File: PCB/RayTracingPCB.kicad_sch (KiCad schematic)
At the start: 8 parts, among them J1 Conn_ARM_JTAG_SWD_10

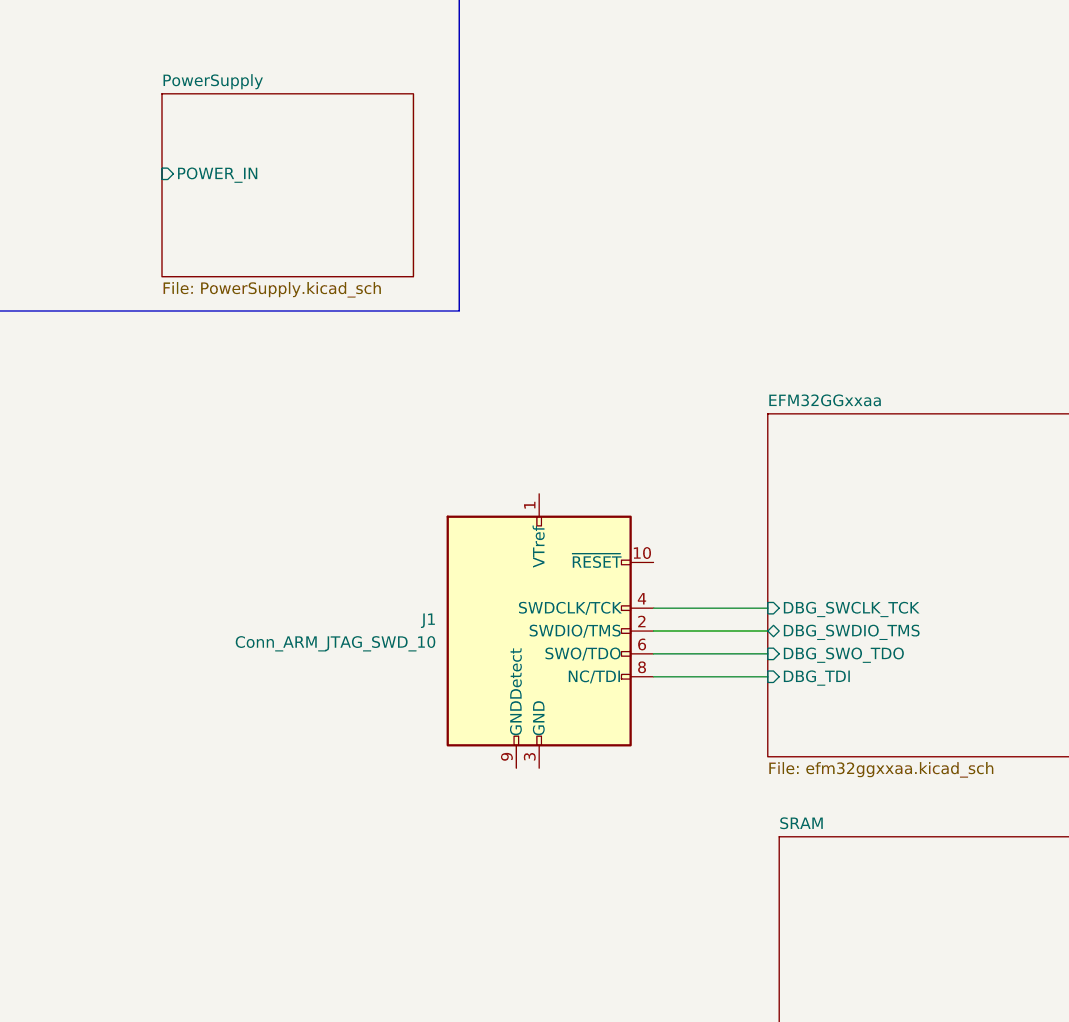
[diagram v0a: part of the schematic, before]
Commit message: add barrel jack
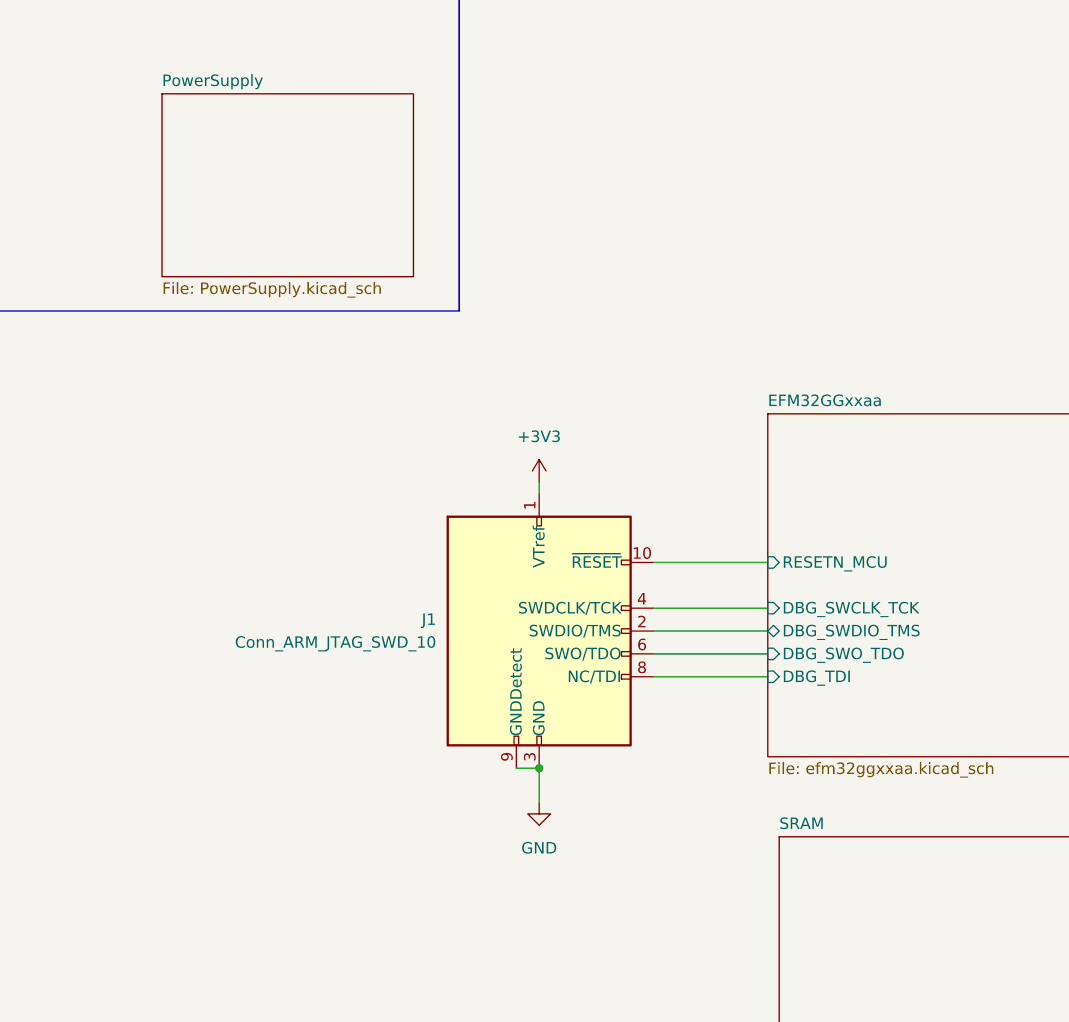
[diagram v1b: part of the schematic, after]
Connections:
- net +3V3: now reaches J1.1 (VTref)
- net EFM32GGxxaa/RESETN_MCU: now reaches J1.10 (~{RESET})
- net GND: now reaches J1.3 (GND), J1.5 (GND)
- net GND: now also J1.9 (GNDDetect)
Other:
- sheet EFM32GGxxaa ports: added RESETN_MCU; removed none
- sheet PowerSupply ports: added none; removed POWER_IN
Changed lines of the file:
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@@
   (junction (at 220.98 90.17) (diameter 0) (color 162 255 50 1)
   )
+  (junction (at 88.9 109.22) (diameter 0) (color 0 0 0 0)
+  )
   (junction (at 218.44 93.98) (diameter 0) (color 0 0 0 0)
   )
@@
   )
   (junction (at 210.82 101.6) (diameter 0) (color 0 0 0 0)
+  )
+  (wire (pts (xy 86.36 109.22) (xy 88.9 109.22))
+    (stroke (width 0) (type default))
   )
   (wire (pts (xy 220.98 90.17) (xy 236.22 90.17))
@@
     (stroke (width 0) (type default))
   )
+  (wire (pts (xy 88.9 77.47) (xy 88.9 78.74))
+    (stroke (width 0) (type default))
+  )
   (wire (pts (xy 213.36 99.06) (xy 236.22 99.06))
     (stroke (width 0) (type default))
@@
     (stroke (width 0) (type default) (color 91 55 255 1))
   )
+  (wire (pts (xy 101.6 86.36) (xy 114.3 86.36))
+    (stroke (width 0) (type default))
+  )
   (wire (pts (xy 220.98 90.17) (xy 220.98 130.81))
     (stroke (width 0) (type default) (color 162 255 50 1))
@@
   (wire (pts (xy 173.99 83.82) (xy 236.22 83.82))
     (stroke (width 0) (type default) (color 91 55 255 1))
+  )
+  (wire (pts (xy 88.9 109.22) (xy 88.9 113.03))
+    (stroke (width 0) (type default))
   )
   (wire (pts (xy 45.72 181.61) (xy 68.58 181.61))
@@
   (label "EMF32GG_QSPI0_IO0" (at 45.72 177.8 0) (fields_autoplaced)
     (effects (font (size 1.27 1.27)) (justify left bottom))
+  )
+  (symbol (lib_id "power:+3V3") (at 88.9 77.47 0) (unit 1)
+    (in_bom yes) (on_board yes) (dnp no) (fields_autoplaced)
+    (property "Reference" "#PWR066" (at 88.9 81.28 0)
+      (effects (font (size 1.27 1.27)) hide)
+    )
+    (property "Value" "+3V3" (at 88.9 72.39 0)
+      (effects (font (size 1.27 1.27)))
+    )
+    (property "Footprint" "" (at 88.9 77.47 0)
+      (effects (font (size 1.27 1.27)) hide)
+    )
+    (property "Datasheet" "" (at 88.9 77.47 0)
+      (effects (font (size 1.27 1.27)) hide)
+    )
+    (pin "1")
+    (instances
+      (project "RayTracingPCB"
+        (path "/e9047d94-28be-4266-894b-6ee25ef088bd"
+          (reference "#PWR066") (unit 1)
+        )
+      )
+    )
+  )
+  (symbol (lib_id "power:GND") (at 88.9 113.03 0) (unit 1)
+    (in_bom yes) (on_board yes) (dnp no) (fields_autoplaced)
+    (property "Reference" "#PWR067" (at 88.9 119.38 0)
+      (effects (font (size 1.27 1.27)) hide)
+    )
+    (property "Value" "GND" (at 88.9 118.11 0)
+      (effects (font (size 1.27 1.27)))
+    )
+    (property "Footprint" "" (at 88.9 113.03 0)
+      (effects (font (size 1.27 1.27)) hide)
+    )
+    (property "Datasheet" "" (at 88.9 113.03 0)
+      (effects (font (size 1.27 1.27)) hide)
+    )
+    (pin "1")
+    (instances
+      (project "RayTracingPCB"
+        (path "/e9047d94-28be-4266-894b-6ee25ef088bd"
+          (reference "#PWR067") (unit 1)
+        )
+      )
+    )
   )
   (symbol (lib_id "Connector:TestPoint_Probe") (at 68.58 185.42 0) (unit 1)
@@
       (effects (font (size 1.27 1.27)) (justify right top) hide)
     )
-    (pin "POWER_IN" input (at 46.99 43.18 180)
-      (effects (font (size 1.27 1.27)) (justify left))
-    )
     (instances
       (project "RayTracingPCB"
@@
       (effects (font (size 1.27 1.27)) (justify right))
     )
-    (instances
+    (pin "RESETN_MCU" input (at 114.3 86.36 180)
+      (effects (font (size 1.27 1.27)) (justify left))
+    )
+    (instances
